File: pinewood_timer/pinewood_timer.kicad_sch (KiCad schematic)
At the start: 1 part, among them U1 STM32F091RCTx

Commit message: worked on schematic more
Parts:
- added C1: .1uF, Capacitor_SMD:C_0805_2012Metric_Pad1.18x1.45mm_HandSolder, symbol Device:C_Small
- added C2: 4.7uF, Capacitor_SMD:C_0805_2012Metric_Pad1.18x1.45mm_HandSolder, symbol Device:C_Small
- added C3, C4, C5, C6, C7: 100nF, Capacitor_SMD:C_0805_2012Metric_Pad1.18x1.45mm_HandSolder, symbol Device:C_Small
- added C8: 1uF, Capacitor_SMD:C_0805_2012Metric_Pad1.18x1.45mm_HandSolder, symbol Device:C_Small
- added PROGRAMMER1: PROGRAMMER, Connector_PinHeader_2.54mm:PinHeader_1x06_P2.54mm_Vertical, symbol Connector:Conn_01x06_Socket
- added RST_Button1: RESET, Button_Switch_SMD:SW_SPST_CK_RS282G05A3, symbol Connector:Conn_01x02_Pin
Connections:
- net +3.3V: now reaches U1.1 (VBAT)
- net +3.3V: now also U1.13 (VDDA), U1.19 (VDD), U1.32 (VDD), U1.64 (VDD), C2.1, C3.1, C4.1, C5.1, C6.1, C7.1, C8.1
- net PC2: now reaches U1.10 (PC2)
- net PC3: now reaches U1.11 (PC3)
- net GND: now reaches U1.12 (VSSA)
- net GND: now also U1.18 (VSS), U1.31 (VSS), U1.47 (VSS), U1.63 (VSS), C1.2, C2.2, C3.2, C4.2, C5.2, C6.2, C7.2, C8.2, PROGRAMMER1.5 (Pin_5), PROGRAMMER1.6 (Pin_6), RST_Button1.2 (Pin_2)
- net PC4: now reaches U1.24 (PC4)
- net PC5: now reaches U1.25 (PC5)
- net PB0: now reaches U1.26 (PB0)
- net PB1: now reaches U1.27 (PB1)
- net PB2: now reaches U1.28 (PB2)
- net PC10: now reaches U1.29 (PB10)
- net PC6: now reaches U1.37 (PC6)
- net PC7: now reaches U1.38 (PC7)
- net PB8: now reaches U1.39 (PC8)
- net PB9: now reaches U1.40 (PC9)
- net PB10: now reaches U1.51 (PC10)
- net PC12 PROGRAMMER: now reaches U1.53 (PC12)
- net PC12 PROGRAMMER: now also PROGRAMMER1.2 (Pin_2)
- net PD2 PROGRAMMER: now reaches U1.54 (PD2)
- net PD2 PROGRAMMER: now also PROGRAMMER1.3 (Pin_3)
- net PB3: now reaches U1.55 (PB3)
- net PB4: now reaches U1.56 (PB4)
- net PB5: now reaches U1.57 (PB5)
- net PB6: now reaches U1.58 (PB6)
- net PB7: now reaches U1.59 (PB7)
- net PC8: now reaches U1.61 (PB8)
- net PC9: now reaches U1.62 (PB9)
- net NRST: now reaches U1.7 (NRST)
- net NRST: now also C1.1, RST_Button1.1 (Pin_1)
- net PC0: now reaches U1.8 (PC0)
- net PC1: now reaches U1.9 (PC1)
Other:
- added sheet power_management (power_management.kicad_sch)
- note added: "4 IR sensors to go under the track. detects if car is above using IR receiver and IR LED. Also has an opamp to make it toggle. might need adc still."
- note added: "4 sets of 4 7-segment displays. displays time to thousandths. goes at the end of the track."
- note added: "4 single 7-segment displays. goes above/below time display. should just display place of each lane."
- note added: "ADC IF NEEDED"
- note added: "LANE PLACEMENT"
- note added: "MUX"
- note added: "Power should come in through a barrel jack for easier use. I should find one with a long cable so it doesn't become a pain. Likely 12v or 5v so should have a linear reg to take the voltage down to 3.3v."
- note added: "Programmer"
- note added: "RESET Button"
- note added: "SHIFT REG"
- note added: "STM REQUIRED"
- note added: "STM power in decoupling caps"
- note added: "TIME DISPLAY LANES 1-2"
- note added: "TIME DISPLAY LANES 3-4"
- moved on the sheet: U1

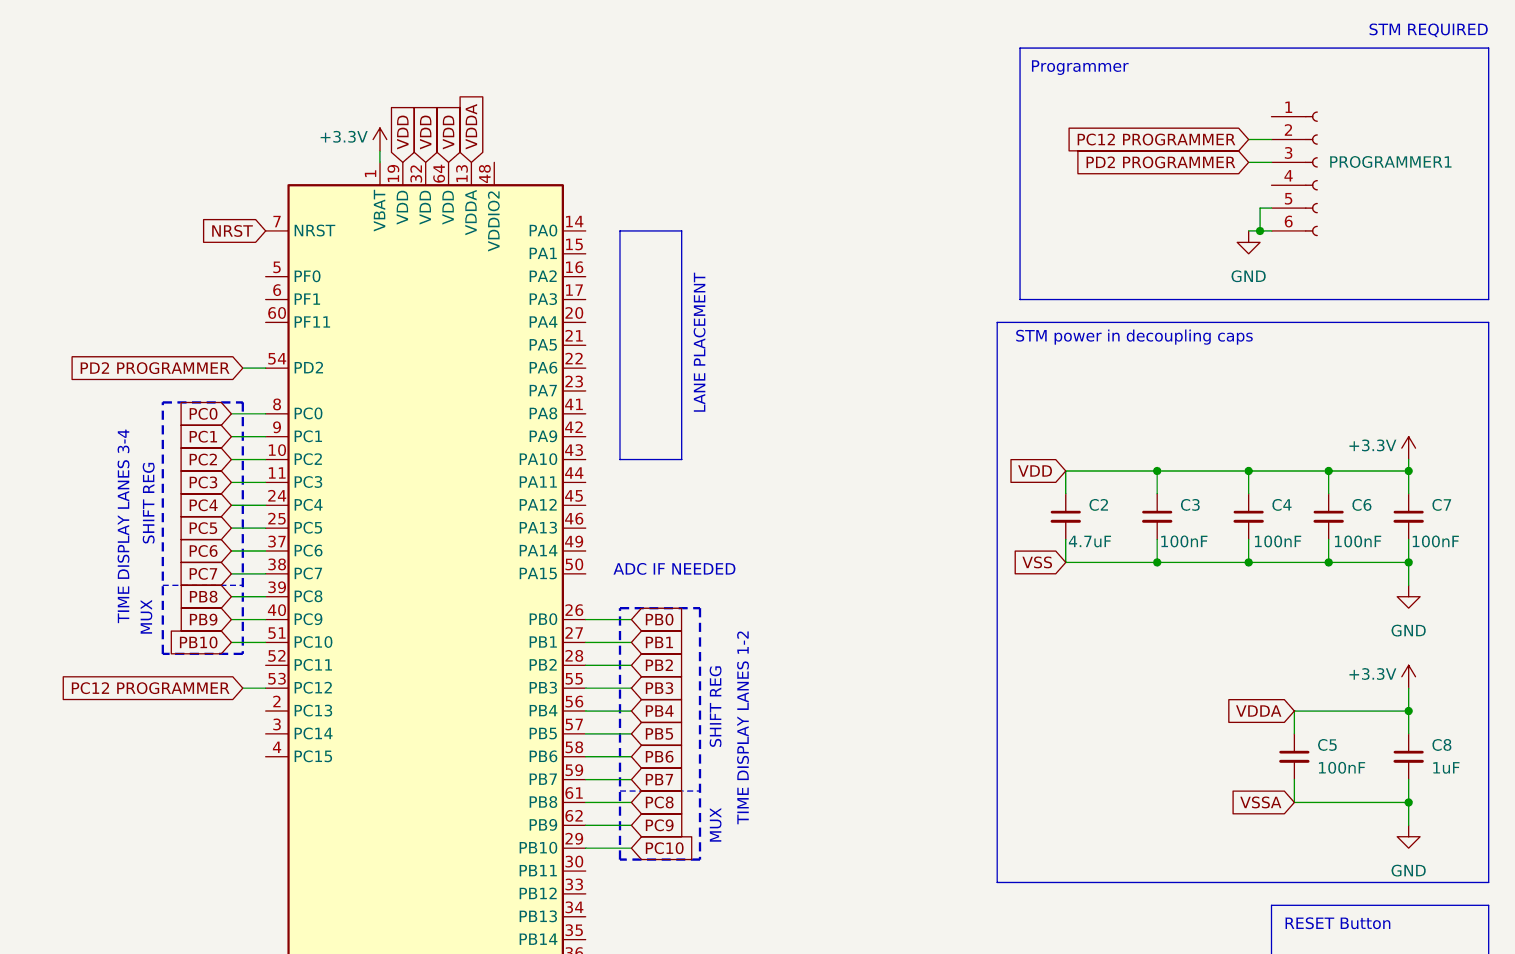
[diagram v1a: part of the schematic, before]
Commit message: edited schematic
added descriptions to sheets
chose sensor pins
added missing items to bom
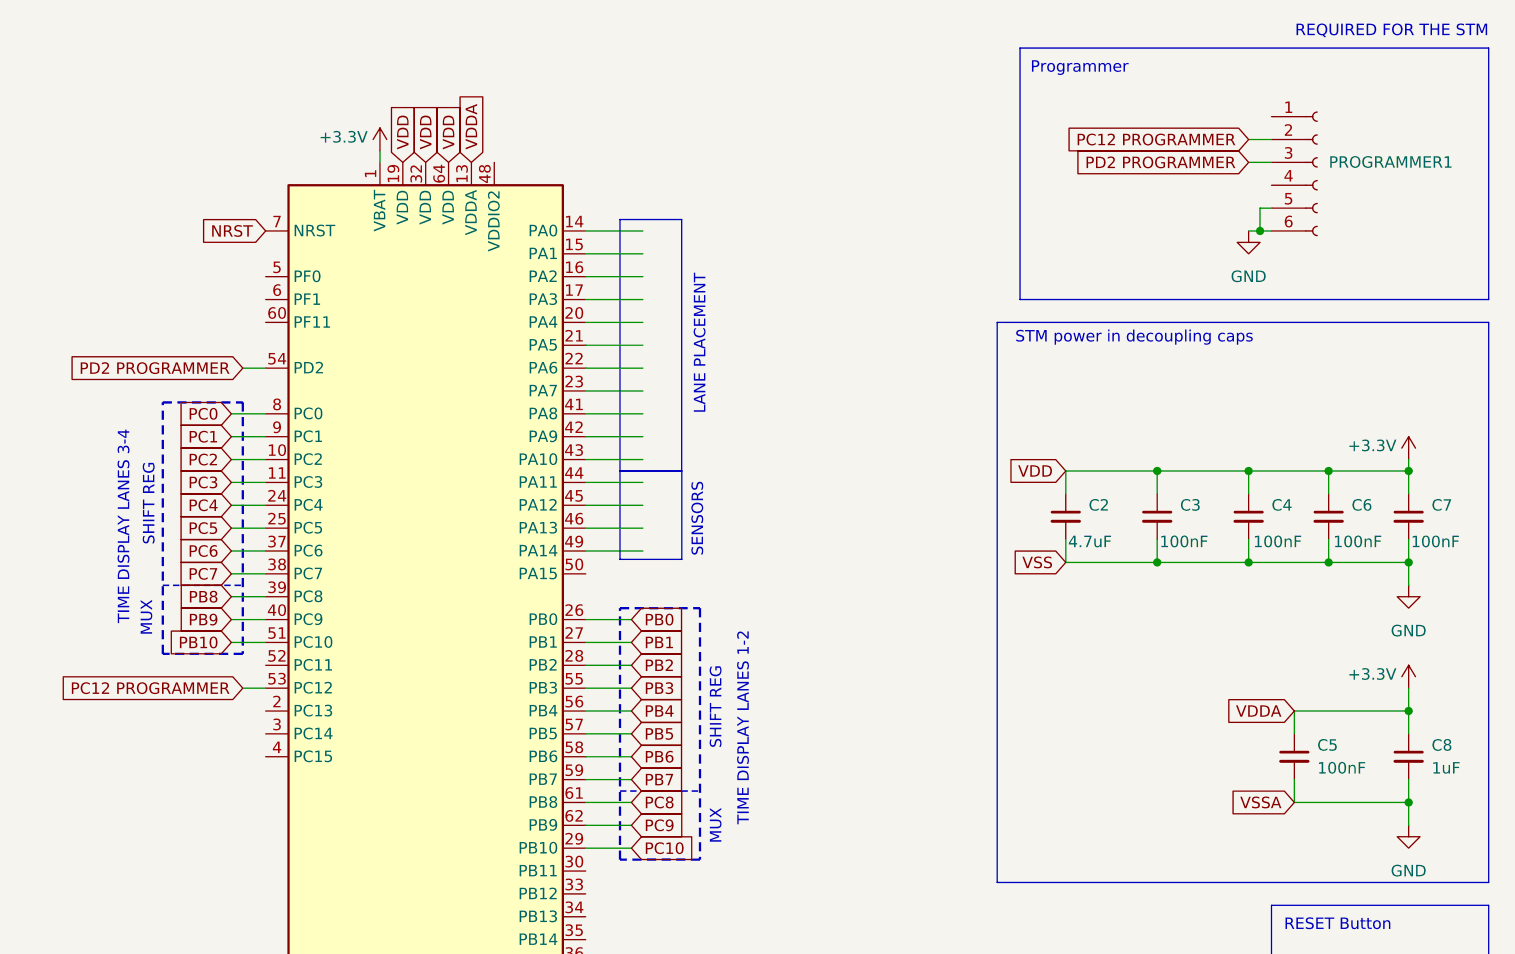
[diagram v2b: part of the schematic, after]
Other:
- note added: "REQUIRED FOR THE STM"
- note added: "SENSORS"
- note removed: "ADC IF NEEDED"
- note removed: "STM REQUIRED"
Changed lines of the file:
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@@
 		)
 		(stroke
-			(width 0)
+			(width 0.1778)
 			(type dash)
 		)
@@
 	(wire
 		(pts
+			(xy 179.07 43.18) (xy 185.42 43.18)
+		)
+		(stroke
+			(width 0)
+			(type default)
+		)
+	)
+	(wire
+		(pts
 			(xy 257.81 99.06) (xy 257.81 101.6)
 		)
@@
 	(wire
 		(pts
+			(xy 179.07 60.96) (xy 185.42 60.96)
+		)
+		(stroke
+			(width 0)
+			(type default)
+		)
+	)
+	(wire
+		(pts
 			(xy 184.15 83.82) (xy 179.07 83.82)
 		)
@@
 	(wire
 		(pts
+			(xy 179.07 68.58) (xy 185.42 68.58)
+		)
+		(stroke
+			(width 0)
+			(type default)
+		)
+	)
+	(wire
+		(pts
 			(xy 252.73 38.1) (xy 254 38.1)
 		)
@@
 	(wire
 		(pts
+			(xy 179.07 71.12) (xy 185.42 71.12)
+		)
+		(stroke
+			(width 0)
+			(type default)
+		)
+	)
+	(wire
+		(pts
+			(xy 179.07 63.5) (xy 185.42 63.5)
+		)
+		(stroke
+			(width 0)
+			(type default)
+		)
+	)
+	(wire
+		(pts
 			(xy 269.24 124.46) (xy 269.24 123.19)
 		)
@@
 	(wire
 		(pts
+			(xy 179.07 66.04) (xy 185.42 66.04)
+		)
+		(stroke
+			(width 0)
+			(type default)
+		)
+	)
+	(wire
+		(pts
 			(xy 184.15 101.6) (xy 179.07 101.6)
 		)
@@
 	(wire
 		(pts
+			(xy 179.07 58.42) (xy 185.42 58.42)
+		)
+		(stroke
+			(width 0)
+			(type default)
+		)
+	)
+	(wire
+		(pts
 			(xy 261.62 64.77) (xy 261.62 67.31)
 		)
@@
 	(wire
 		(pts
+			(xy 179.07 50.8) (xy 185.42 50.8)
+		)
+		(stroke
+			(width 0)
+			(type default)
+		)
+	)
+	(wire
+		(pts
 			(xy 140.97 53.34) (xy 143.51 53.34)
 		)
@@
 		)
 		(stroke
-			(width 0)
+			(width 0.1778)
 			(type dash)
 		)
@@
 	(wire
 		(pts
+			(xy 179.07 48.26) (xy 185.42 48.26)
+		)
+		(stroke
+			(width 0)
+			(type default)
+		)
+	)
+	(wire
+		(pts
 			(xy 270.51 104.14) (xy 270.51 101.6)
 		)
@@
 	(wire
 		(pts
+			(xy 179.07 40.64) (xy 185.42 40.64)
+		)
+		(stroke
+			(width 0)
+			(type default)
+		)
+	)
+	(wire
+		(pts
+			(xy 179.07 38.1) (xy 185.42 38.1)
+		)
+		(stroke
+			(width 0)
+			(type default)
+		)
+	)
+	(wire
+		(pts
 			(xy 254 35.56) (xy 254 38.1)
 		)
@@
 	(wire
 		(pts
+			(xy 179.07 73.66) (xy 185.42 73.66)
+		)
+		(stroke
+			(width 0)
+			(type default)
+		)
+	)
+	(wire
+		(pts
 			(xy 139.7 63.5) (xy 143.51 63.5)
 		)
@@
 	(wire
 		(pts
+			(xy 179.07 55.88) (xy 185.42 55.88)
+		)
+		(stroke
+			(width 0)
+			(type default)
+		)
+	)
+	(wire
+		(pts
+			(xy 179.07 53.34) (xy 185.42 53.34)
+		)
+		(stroke
+			(width 0)
+			(type default)
+		)
+	)
+	(wire
+		(pts
 			(xy 270.51 88.9) (xy 270.51 91.44)
 		)
@@
 		(pts
 			(xy 270.51 64.77) (xy 270.51 67.31)
+		)
+		(stroke
+			(width 0)
+			(type default)
+		)
+	)
+	(wire
+		(pts
+			(xy 179.07 45.72) (xy 185.42 45.72)
 		)
 		(stroke
@@
 	)
 	(rectangle
+		(start 182.88 64.77)
+		(end 189.7433 74.5907)
+		(stroke
+			(width 0)
+			(type default)
+		)
+		(fill
+			(type none)
+		)
+	)
+	(rectangle
 		(start 255.27 113.03)
 		(end 279.4 135.89)
@@
 	)
 	(rectangle
-		(start 182.88 38.1)
-		(end 189.738 63.5)
+		(start 182.88 36.83)
+		(end 189.738 64.77)
 		(stroke
 			(width 0)
@@
 		)
 	)
-	(text "STM REQUIRED"
+	(text "REQUIRED FOR THE STM\n"
 		(exclude_from_sim no)
 		(at 279.4 16.002 0)
@@
 		)
 	)
-	(text "ADC IF NEEDED"
-		(exclude_from_sim no)
-		(at 188.976 75.946 0)
-		(effects
-			(font
-				(size 1.27 1.27)
-			)
-		)
-	)
 	(text "MUX"
 		(exclude_from_sim no)
@@
 		)
 	)
+	(text "SENSORS"
+		(exclude_from_sim no)
+		(at 191.516 74.422 90)
+		(effects
+			(font
+				(size 1.27 1.27)
+			)
+			(justify left)
+		)
+	)

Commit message: added pins
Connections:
- net V_OUT1: now reaches U1.44 (PA11)
- net V_OUT2: now reaches U1.45 (PA12)
- net V_OUT3: now reaches U1.46 (PA13)
- net V_OUT4: now reaches U1.49 (PA14)
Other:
- note added: "(INPUT)"
- note added: "(OUTPUT)"
- note added: "PA10-14 input to read if car/not"
- note added: "PC0-7 output shift reg PC8-10 mux PB0-7 output shift reg PB8-10 mux"
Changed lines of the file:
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@@
 	(wire
 		(pts
-			(xy 179.07 68.58) (xy 185.42 68.58)
+			(xy 179.07 68.58) (xy 184.15 68.58)
 		)
 		(stroke
@@
 	(wire
 		(pts
-			(xy 179.07 71.12) (xy 185.42 71.12)
+			(xy 179.07 71.12) (xy 184.15 71.12)
 		)
 		(stroke
@@
 	(wire
 		(pts
-			(xy 179.07 66.04) (xy 185.42 66.04)
+			(xy 179.07 66.04) (xy 184.15 66.04)
 		)
 		(stroke
@@
 	(wire
 		(pts
-			(xy 179.07 73.66) (xy 185.42 73.66)
+			(xy 179.07 73.66) (xy 184.15 73.66)
 		)
 		(stroke
@@
 	(rectangle
 		(start 182.88 64.77)
-		(end 189.7433 74.5907)
-		(stroke
-			(width 0)
+		(end 194.31 74.93)
+		(stroke
+			(width 0.254)
 			(type default)
 		)
@@
 	(rectangle
 		(start 182.88 36.83)
-		(end 189.738 64.77)
-		(stroke
-			(width 0)
+		(end 194.31 64.77)
+		(stroke
+			(width 0.254)
 			(type default)
 		)
@@
 		)
 	)
+	(text "(OUTPUT)\n"
+		(exclude_from_sim no)
+		(at 198.12 50.8 90)
+		(effects
+			(font
+				(size 1.27 1.27)
+			)
+		)
+	)
 	(text "REQUIRED FOR THE STM\n"
 		(exclude_from_sim no)
@@
 		)
 	)
+	(text "(INPUT)\n"
+		(exclude_from_sim no)
+		(at 197.358 69.596 90)
+		(effects
+			(font
+				(size 1.27 1.27)
+			)
+		)
+	)
+	(text "PC0-7 output shift reg\nPC8-10 mux\nPB0-7 output shift reg\nPB8-10 mux\n"
+		(exclude_from_sim no)
+		(at 20.32 92.71 0)
+		(effects
+			(font
+				(size 1.27 1.27)
+			)
+			(justify left bottom)
+		)
+	)
 	(text "MUX"
 		(exclude_from_sim no)
@@
 	(text "LANE PLACEMENT"
 		(exclude_from_sim no)
-		(at 191.77 50.8 90)
+		(at 195.58 51.054 90)
 		(effects
 			(font
@@
 	(text "SENSORS"
 		(exclude_from_sim no)
-		(at 191.516 74.422 90)
-		(effects
-			(font
-				(size 1.27 1.27)
-			)
-			(justify left)
+		(at 195.58 74.422 90)
+		(effects
+			(font
+				(size 1.27 1.27)
+			)
+			(justify left)
+		)
+	)
+	(text "(OUTPUT)\n"
+		(exclude_from_sim no)
+		(at 199.136 93.726 90)
+		(effects
+			(font
+				(size 1.27 1.27)
+			)
+		)
+	)
+	(text "PA10-14 input to read if car/not"
+		(exclude_from_sim no)
+		(at 20.32 66.04 0)
+		(effects
+			(font
+				(size 1.27 1.27)
+			)
+			(justify left bottom)
 		)
 	)
@@
 		)
 	)
+	(text "(OUTPUT)\n"
+		(exclude_from_sim no)
+		(at 125.476 71.374 90)
+		(effects
+			(font
+				(size 1.27 1.27)
+			)
+		)
+	)
 	(text "SHIFT REG"
 		(exclude_from_sim no)
@@
 		)
 	)
+	(global_label "V_OUT2"
+		(shape input)
+		(at 184.15 68.58 0)
+		(fields_autoplaced yes)
+		(effects
+			(font
+				(size 1.27 1.27)
+			)
+			(justify left)
+		)
+		(property "Intersheetrefs" "${INTERSHEET_REFS}"
+			(at 194.0295 68.58 0)
+			(effects
+				(font
+					(size 1.27 1.27)
+				)
+				(justify left)
+				(hide yes)
+			)
+		)
+	)
 	(global_label "VSS"
 		(shape input)
@@
 		)
 	)
+	(global_label "V_OUT1"
+		(shape input)
+		(at 184.15 66.04 0)
+		(fields_autoplaced yes)
+		(effects
+			(font
+				(size 1.27 1.27)
+			)
+			(justify left)
+		)
+		(property "Intersheetrefs" "${INTERSHEET_REFS}"
+			(at 194.0295 66.04 0)
+			(effects
+				(font
+					(size 1.27 1.27)
+				)
+				(justify left)
+				(hide yes)
+			)
+		)
+	)
 	(global_label "PB0"
 		(shape input)
@@
 		)
 	)
+	(global_label "V_OUT3"
+		(shape input)
+		(at 184.15 71.12 0)
+		(fields_autoplaced yes)
+		(effects
+			(font
+				(size 1.27 1.27)
+			)
+			(justify left)
+		)
+		(property "Intersheetrefs" "${INTERSHEET_REFS}"
+			(at 194.0295 71.12 0)
+			(effects
+				(font
+					(size 1.27 1.27)
+				)
+				(justify left)
+				(hide yes)
+			)
+		)
+	)
 	(global_label "PC7"
 		(shape input)
@@
 				(hide yes)
 			)
+		)
+	)
+	(global_label "V_OUT4"
+		(shape input)
+		(at 184.15 73.66 0)
+		(fields_autoplaced yes)
+		(effects
+			(font
+				(size 1.27 1.27)
+			)
+			(justify left)
+		)
+		(property "Intersheetrefs" "${INTERSHEET_REFS}"
+			(at 194.0295 73.66 0)
+			(effects
+				(font
+					(size 1.27 1.27)
+				)
+				(justify left)
+				(hide yes)
+			)
